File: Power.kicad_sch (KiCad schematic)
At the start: 10 parts, among them J1 303C-C4115-30-04, P1 PHR-2, U2 TPS7A2033PDBVR, U3 TPS22918DBVR

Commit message: new rect version
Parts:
- U3: footprint LightFusion:TPS22918DBVR-6N -> LightFusion:TPS22918DBVT; symbol TPS22918DBVR:TPS22918DBVR -> TPS22918DBVT:TPS22918DBVT; Height (none) -> 1.45; Manufacturer_Name (none) -> Texas Instruments; Manufacturer_Part_Number (none) -> TPS22918DBVT; Mouser Part Number (none) -> 595-TPS22918DBVT; Mouser Price/Stock (none) -> https://www.mouser.co.uk/ProductDetail/Texas-Instruments/TP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
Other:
- moved on the sheet: C25, U3
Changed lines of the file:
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@@
+	)
+	(junction
+		(at 110.49 127)
+		(diameter 0)
+		(color 0 0 0 0)
 	)
 	(junction
@@
 	)
 	(junction
-		(at 110.49 118.11)
+		(at 149.86 121.92)
 		(diameter 0)
 		(color 0 0 0 0)
@@
 	(wire
 		(pts
+			(xy 110.49 127) (xy 110.49 142.24)
+		)
+		(stroke
+			(width 0)
+			(type default)
+		)
+	)
+	(wire
+		(pts
 			(xy 138.43 137.16) (xy 100.33 137.16)
 		)
@@
 	(wire
 		(pts
+			(xy 149.86 121.92) (xy 149.86 124.46)
+		)
+		(stroke
+			(width 0)
+			(type default)
+		)
+	)
+	(wire
+		(pts
 			(xy 54.61 102.87) (xy 54.61 107.95)
 		)
@@
 	(wire
 		(pts
+			(xy 146.05 124.46) (xy 149.86 124.46)
+		)
+		(stroke
+			(width 0)
+			(type default)
+		)
+	)
+	(wire
+		(pts
 			(xy 110.49 118.11) (xy 107.95 118.11)
 		)
@@
 	(wire
 		(pts
-			(xy 114.3 118.11) (xy 110.49 118.11)
-		)
-		(stroke
-			(width 0)
-			(type default)
-		)
-	)
-	(wire
-		(pts
 			(xy 167.64 72.39) (xy 171.45 72.39)
 		)
@@
 	(wire
 		(pts
+			(xy 114.3 120.65) (xy 114.3 121.92)
+		)
+		(stroke
+			(width 0)
+			(type default)
+		)
+	)
+	(wire
+		(pts
 			(xy 100.33 137.16) (xy 100.33 120.65)
 		)
@@
 	(wire
 		(pts
-			(xy 149.86 120.65) (xy 149.86 123.19)
+			(xy 149.86 120.65) (xy 149.86 121.92)
 		)
 		(stroke
@@
 	(wire
 		(pts
+			(xy 114.3 121.92) (xy 118.11 121.92)
+		)
+		(stroke
+			(width 0)
+			(type default)
+		)
+	)
+	(wire
+		(pts
 			(xy 100.33 92.71) (xy 100.33 96.52)
 		)
@@
 	(wire
 		(pts
+			(xy 110.49 127) (xy 118.11 127)
+		)
+		(stroke
+			(width 0)
+			(type default)
+		)
+	)
+	(wire
+		(pts
+			(xy 146.05 121.92) (xy 149.86 121.92)
+		)
+		(stroke
+			(width 0)
+			(type default)
+		)
+	)
+	(wire
+		(pts
 			(xy 100.33 96.52) (xy 100.33 120.65)
 		)
@@
 	(wire
 		(pts
-			(xy 110.49 118.11) (xy 110.49 142.24)
+			(xy 110.49 118.11) (xy 110.49 127)
 		)
 		(stroke
@@
 	(global_label "GND"
 		(shape input)
-		(at 149.86 130.81 0)
+		(at 118.11 124.46 180)
 		(fields_autoplaced yes)
 		(effects
@@
 				(size 1.27 1.27)
 			)
-			(justify left)
+			(justify right)
 		)
 		(property "Intersheetrefs" "${INTERSHEET_REFS}"
-			(at 156.7157 130.81 0)
-			(hide yes)
-			(show_name no)
-			(do_not_autoplace no)
-			(effects
-				(font
-					(size 1.27 1.27)
-				)
-				(justify left)
+			(at 111.2543 124.46 0)
+			(hide yes)
+			(show_name no)
+			(do_not_autoplace no)
+			(effects
+				(font
+					(size 1.27 1.27)
+				)
+				(justify right)
 			)
 		)
@@
 	(global_label "GND"
 		(shape input)
-		(at 149.86 111.76 90)
+		(at 151.13 127 0)
 		(fields_autoplaced yes)
 		(effects
@@
 		)
 		(property "Intersheetrefs" "${INTERSHEET_REFS}"
-			(at 149.86 104.9043 90)
+			(at 157.9857 127 0)
 			(hide yes)
 			(show_name no)
@@
 	)
 	(symbol
-		(lib_id "TPS22918DBVR:TPS22918DBVR")
-		(at 132.08 125.73 0)
+		(lib_id "TPS22918DBVT:TPS22918DBVT")
+		(at 118.11 121.92 0)
 		(unit 1)
 		(body_style 1)
@@
 		(fields_autoplaced yes)
 		(property "Reference" "U3"
-			(at 132.08 110.49 0)
+			(at 132.08 114.3 0)
 			(show_name no)
 			(do_not_autoplace no)
@@
 		)
 		(property "Value" "TPS22918DBVR"
-			(at 132.08 113.03 0)
-			(show_name no)
-			(do_not_autoplace no)
-			(effects
-				(font
-					(size 1.27 1.27)
-				)
-			)
-		)
-		(property "Footprint" "LightFusion:TPS22918DBVR-6N"
-			(at 132.08 125.73 0)
-			(hide yes)
-			(show_name no)
-			(do_not_autoplace no)
-			(effects
-				(font
-					(size 1.27 1.27)
-				)
-				(justify bottom)
-			)
-		)
-		(property "Datasheet" ""
-			(at 132.08 125.73 0)
-			(hide yes)
-			(show_name no)
-			(do_not_autoplace no)
-			(effects
-				(font
-					(size 1.27 1.27)
-				)
-			)
-		)
-		(property "Description" ""
-			(at 132.08 125.73 0)
-			(hide yes)
-			(show_name no)
-			(do_not_autoplace no)
-			(effects
-				(font
-					(size 1.27 1.27)
-				)
+			(at 132.08 116.84 0)
+			(show_name no)
+			(do_not_autoplace no)
+			(effects
+				(font
+					(size 1.27 1.27)
+				)
+			)
+		)
+		(property "Footprint" "LightFusion:TPS22918DBVT"
+			(at 142.24 216.84 0)
+			(hide yes)
+			(show_name no)
+			(do_not_autoplace no)
+			(effects
+				(font
+					(size 1.27 1.27)
+				)
+				(justify left top)
+			)
+		)
+		(property "Datasheet" "http://www.ti.com/lit/gpn/tps22918"
+			(at 142.24 316.84 0)
+			(hide yes)
+			(show_name no)
+			(do_not_autoplace no)
+			(effects
+				(font
+					(size 1.27 1.27)
+				)
+				(justify left top)
+			)
+		)
+		(property "Description" "5.5V, 2A, 52m Load Switch with Adjustable Rise Time and Adjustable Quick Output Discharge"
+			(at 118.11 121.92 0)
+			(hide yes)
+			(show_name no)
+			(do_not_autoplace no)
+			(effects
+				(font
+					(size 1.27 1.27)
+				)
+			)
+		)
+		(property "Height" "1.45"
+			(at 142.24 516.84 0)
+			(hide yes)
+			(show_name no)
+			(do_not_autoplace no)
+			(effects
+				(font
+					(size 1.27 1.27)
+				)
+				(justify left top)
+			)
+		)
+		(property "Mouser Part Number" "595-TPS22918DBVT"
+			(at 142.24 616.84 0)
+			(hide yes)
+			(show_name no)
+			(do_not_autoplace no)
+			(effects
+				(font
+					(size 1.27 1.27)
+				)
+				(justify left top)
+			)
+		)
+		(property "Mouser Price/Stock" "https://www.mouser.co.uk/ProductDetail/Texas-Instruments/TPS22918DBVT?qs=f4l5qYp%2Fy%252B5OmR4LO0ZvPg%3D%3D"
+			(at 142.24 716.84 0)
+			(hide yes)
+			(show_name no)
+			(do_not_autoplace no)
+			(effects
+				(font
+					(size 1.27 1.27)
+				)
+				(justify left top)
+			)
+		)
+		(property "Manufacturer_Name" "Texas Instruments"
+			(at 142.24 816.84 0)
+			(hide yes)
+			(show_name no)
+			(do_not_autoplace no)
+			(effects
+				(font
+					(size 1.27 1.27)
+				)
+				(justify left top)
+			)
+		)
+		(property "Manufacturer_Part_Number" "TPS22918DBVT"
+			(at 142.24 916.84 0)
+			(hide yes)
+			(show_name no)
+			(do_not_autoplace no)
+			(effects
+				(font
+					(size 1.27 1.27)
+				)
+				(justify left top)
 			)
 		)
@@
 	(symbol
 		(lib_id "C_Small_US:C_Small_US")
-		(at 149.86 114.3 0)
+		(at 148.59 127 270)
 		(unit 1)
 		(body_style 1)
@@
 		(fields_autoplaced yes)
 		(property "Reference" "C25"
-			(at 152.4 114.4269 0)
+			(at 148.4631 129.54 0)
 			(show_name no)
 			(do_not_autoplace no)
@@
 		)
 		(property "Value" "1 nF"
-			(at 152.4 115.6969 0)
+			(at 147.1931 129.54 0)
 			(hide yes)
 			(show_name no)
@@
 		)
 		(property "Footprint" "LightFusion:C_0603_1608Metric"
-			(at 149.86 114.3 0)
+			(at 148.59 127 0)
 			(hide yes)
 			(show_name no)
@@
 		)
 		(property "Datasheet" ""
-			(at 149.86 114.3 0)
+			(at 148.59 127 0)
 			(hide yes)
 			(show_name no)
@@
 		)
 		(property "Description" "C0G/NP0 preferred; X7R acceptable"
-			(at 149.86 114.3 0)
-			(hide yes)
-			(show_name no)
+			(at 148.59 127 0)
+			(hide yes)
+			(show_name no)

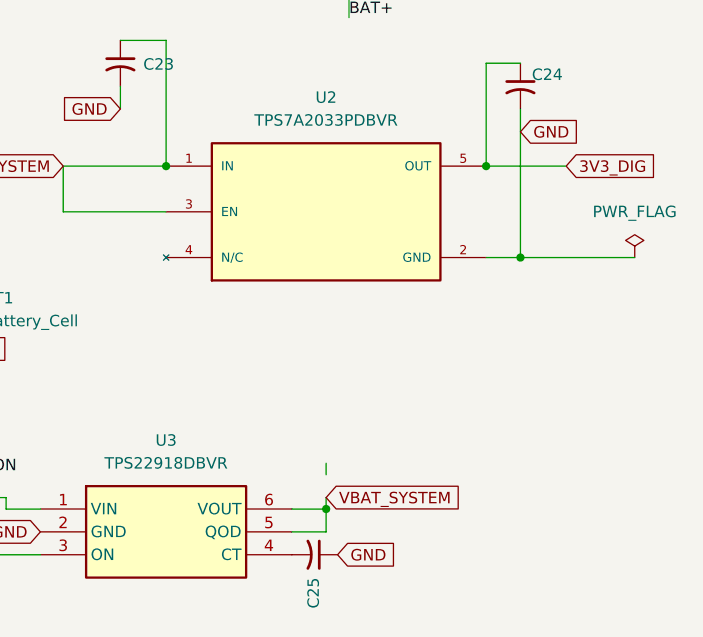
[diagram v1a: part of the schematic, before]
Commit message: routing ready DRC passed
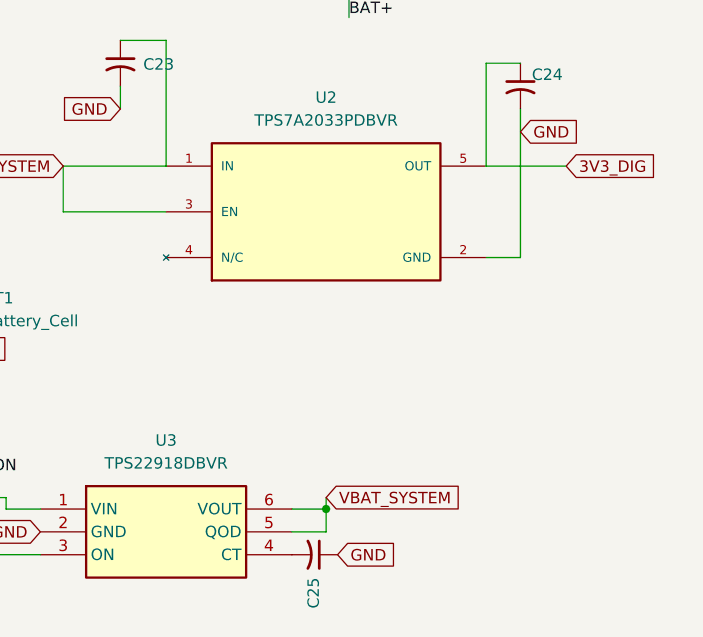
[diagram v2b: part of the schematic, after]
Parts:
- U3: footprint LightFusion:TPS22918DBVT -> LightFusion:TPS22918DBVR-6N
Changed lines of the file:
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@@
 	(paper "A4")
-	(junction
-		(at 132.08 83.82)
-		(diameter 0)
-		(color 0 0 0 0)
-	)
-	(junction
-		(at 167.64 83.82)
-		(diameter 0)
-		(color 0 0 0 0)
-	)
 	(junction
 		(at 110.49 127)
@@
 	)
 	(junction
-		(at 171.45 93.98)
-		(diameter 0)
-		(color 0 0 0 0)
-	)
-	(junction
 		(at 100.33 120.65)
 		(diameter 0)
@@
 	(wire
 		(pts
-			(xy 171.45 93.98) (xy 184.15 93.98)
-		)
-		(stroke
-			(width 0)
-			(type default)
-		)
-	)
-	(wire
-		(pts
 			(xy 107.95 118.11) (xy 107.95 114.3)
 		)
@@
 	(wire
 		(pts
-			(xy 149.86 116.84) (xy 149.86 118.11)
+			(xy 146.05 121.92) (xy 149.86 121.92)
 		)
 		(stroke
@@
 		(pts
 			(xy 110.49 127) (xy 118.11 127)
-		)
-		(stroke
-			(width 0)
-			(type default)
-		)
-	)
-	(wire
-		(pts
-			(xy 146.05 121.92) (xy 149.86 121.92)
 		)
 		(stroke
@@
 				)
 				(justify right)
-			)
-		)
-	)
-	(symbol
-		(lib_id "PWR_FLAG:PWR_FLAG")
-		(at 184.15 93.98 0)
-		(unit 1)
-		(body_style 1)
-		(exclude_from_sim no)
-		(in_bom yes)
-		(on_board yes)
-		(in_pos_files yes)
-		(dnp no)
-		(fields_autoplaced yes)
-		(property "Reference" "#FLG04"
-			(at 184.15 92.075 0)
-			(hide yes)
-			(show_name no)
-			(do_not_autoplace no)
-			(effects
-				(font
-					(size 1.27 1.27)
-				)
-			)
-		)
-		(property "Value" "PWR_FLAG"
-			(at 184.15 88.9 0)
-			(show_name no)
-			(do_not_autoplace no)
-			(effects
-				(font
-					(size 1.27 1.27)
-				)
-			)
-		)
-		(property "Footprint" ""
-			(at 184.15 93.98 0)
-			(hide yes)
-			(show_name no)
-			(do_not_autoplace no)
-			(effects
-				(font
-					(size 1.27 1.27)
-				)
-			)
-		)
-		(property "Datasheet" ""
-			(at 184.15 93.98 0)
-			(hide yes)
-			(show_name no)
-			(do_not_autoplace no)
-			(effects
-				(font
-					(size 1.27 1.27)
-				)
-			)
-		)
-		(property "Description" "Special symbol for telling ERC where power comes from"
-			(at 184.15 93.98 0)
-			(hide yes)
-			(show_name no)
-			(do_not_autoplace no)
-			(effects
-				(font
-					(size 1.27 1.27)
-				)
-			)
-		)
-		(pin "1"
-		)
-		(instances
-			(project "LightFusion"
-				(path "/1aacc45f-6fcc-4559-bec0-55c6f50555c1/5e0cd53b-8700-46c2-b7ce-d555894c5a40"
-					(reference "#FLG04")
-					(unit 1)
-				)
-			)
-			(project "Power"
-				(path "/fd4ff215-173a-45ff-8b17-686d5a17abc7"
-					(reference "#FLG04")
-					(unit 1)
-				)
 			)
 		)
@@
 			)
 		)
-		(property "Footprint" "LightFusion:TPS22918DBVT"
+		(property "Footprint" "LightFusion:TPS22918DBVR-6N"
 			(at 142.24 216.84 0)
 			(hide yes)
